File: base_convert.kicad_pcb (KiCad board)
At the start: 2 copper layers, 93.3 x 100 mm, 96 parts, among them J1 ISP, J3 Vin, Q1 Q_PMOS_GSD, Q10 Q_PNP_BEC, Q11 Q_PNP_BEC, Q12 Q_PNP_BEC, Q13 Q_PNP_BEC, Q14 Q_PNP_BEC, Q15 Q_PNP_BEC, Q16 Q_PNP_BEC, Q17 Q_PNP_BEC, Q18 Q_PNP_BEC, Q19 Q_PNP_BEC, Q2 Q_PNP_BEC, Q20 Q_NPN_BEC, Q21 Q_NPN_BEC, Q22 Q_NPN_BEC, Q23 Q_NPN_BEC, Q24 Q_NPN_BEC, Q25 Q_NPN_BEC, Q26 Q_NPN_BEC, Q27 Q_NPN_BEC, Q3 Q_PNP_BEC, Q4 Q_PNP_BEC, Q5 Q_PNP_BEC, Q6 Q_NPN_BEC, Q7 Q_NPN_BEC, Q8 Q_NPN_BEC, Q9 Q_NPN_BEC, SW1 SELECT, SW10 1, SW11 4, SW12 7, SW13 A, SW14 CLEAR, SW15 B, SW16 C, SW17 D, SW18 E, SW2 3, SW3 6, SW4 9, SW5 F, SW6 2, SW7 5, SW8 8, SW9 0, U1 MIC5317-3.3YM5-TR, U2 MSP430FR2033IPMR

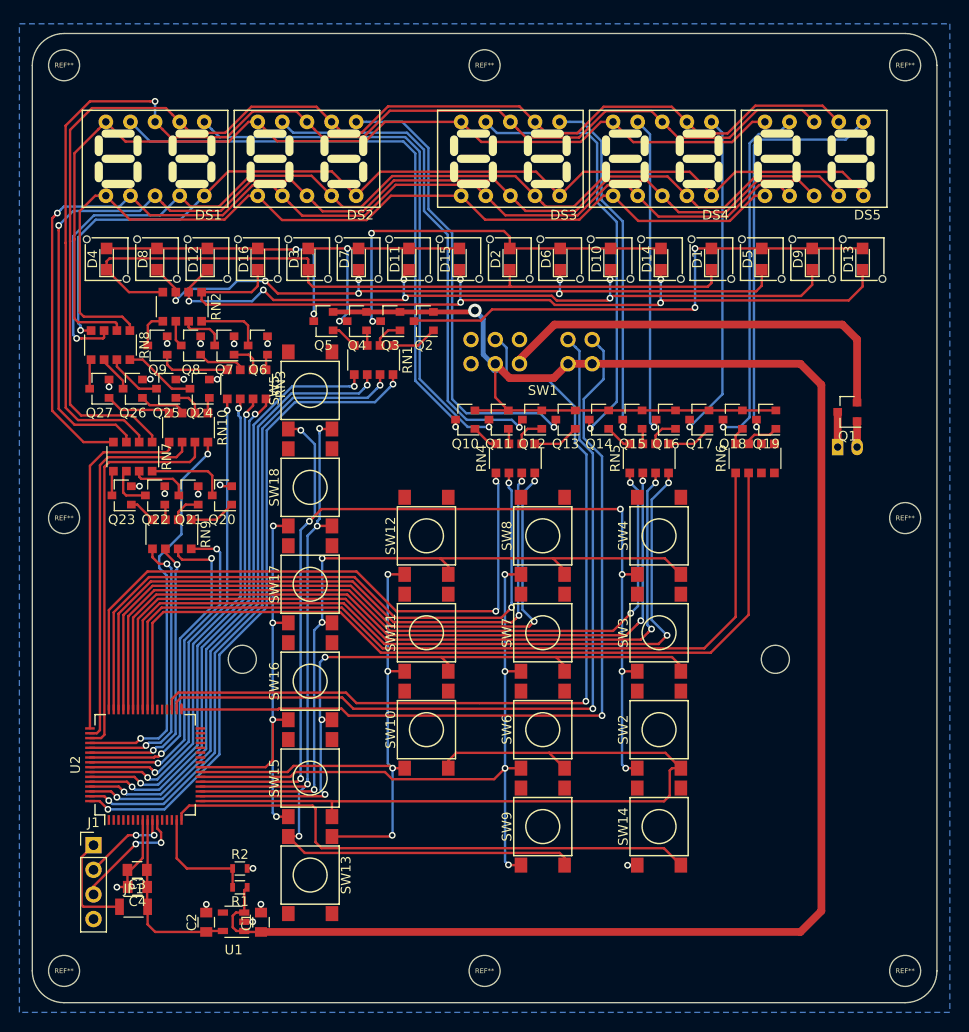
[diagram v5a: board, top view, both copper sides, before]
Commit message: change pcb standoof from 3mm to 2.5mm
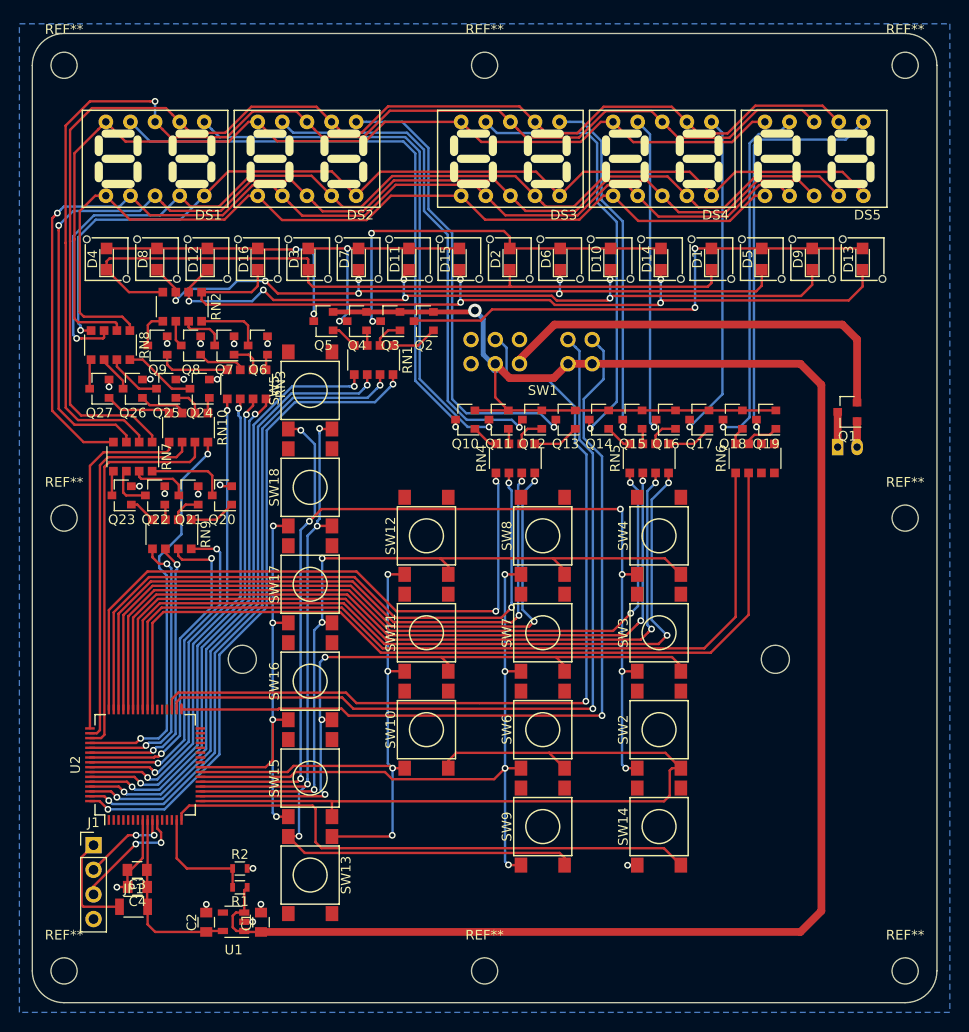
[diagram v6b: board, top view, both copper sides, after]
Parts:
- removed the REF** at (143.4, 100.0)
- removed the REF** at (100.0, 53.3)
- removed the REF** at (56.6, 100.0)
- removed the REF** at (100.0, 146.7)
- removed the REF** at (56.6, 146.7)
- removed the REF** at (143.4, 146.7)
- removed the REF** at (143.4, 53.3)
- removed the REF** at (56.6, 53.3)
- added REF**: MountingHole_2.7mm_M2.5, Mounting_Holes:MountingHole_2.7mm_M2.5, F.Cu at (56.6, 100.0)
- added REF**: MountingHole_2.7mm_M2.5, Mounting_Holes:MountingHole_2.7mm_M2.5, F.Cu at (56.6, 146.7)
- added REF**: MountingHole_2.7mm_M2.5, Mounting_Holes:MountingHole_2.7mm_M2.5, F.Cu at (100.0, 146.7)
- added REF**: MountingHole_2.7mm_M2.5, Mounting_Holes:MountingHole_2.7mm_M2.5, F.Cu at (143.4, 146.7)
- added REF**: MountingHole_2.7mm_M2.5, Mounting_Holes:MountingHole_2.7mm_M2.5, F.Cu at (143.4, 100.0)
- added REF**: MountingHole_2.7mm_M2.5, Mounting_Holes:MountingHole_2.7mm_M2.5, F.Cu at (143.4, 53.3)
- added REF**: MountingHole_2.7mm_M2.5, Mounting_Holes:MountingHole_2.7mm_M2.5, F.Cu at (100.0, 53.3)
- added REF**: MountingHole_2.7mm_M2.5, Mounting_Holes:MountingHole_2.7mm_M2.5, F.Cu at (56.6, 53.3)
